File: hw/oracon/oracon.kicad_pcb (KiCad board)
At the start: 2 copper layers, 100 x 134.6 mm, 102 parts, among them J1 DE9_Pins_MountingHoles, J2 SIM_Card, J3 USB_A, J4 Conn_02x20_Odd_Even, J5 USB_C_Receptacle_USB2.0_16P, Q1 SS8050, Q2 SS8050, Q3 SS8050, Q5 SS8050, SW1 SW_Push, U1 TP5100, U2 AMS1117-3.3, U3 ESP32-S3-MINI-1U, U4 CH343P, U5 TPS61022, U6 MAX3232, U7 SIM7022

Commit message: Work on PCB, renamed KiCad project
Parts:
- removed J4: Conn_02x20_Odd_Even, Connector_PinHeader_2.54mm:PinHeader_2x20_P2.54mm_Vertical
- J3: footprint Connector_USB:USB_A_Molex_67643_Horizontal -> kolskypavel:HYC214-USBA04-113; moved to B.Cu
- J5, U7: moved to B.Cu
- moved SW1 180.0 mm to (8.00, 103.5)
- moved J2 174.1 mm to (-5.75, 97.2), turned to 90 degrees
- moved D6 169.4 mm to (7.79, 98.8)
- moved D4 127.3 mm to (-33.0, 83.5), turned to 90 degrees
- moved D3 125.9 mm to (-33.0, 75.2), turned to 90 degrees
- moved D2 124.0 mm to (-32.8, 66.5), turned to 90 degrees
- moved U3 116.7 mm to (2.15, 94.0)
- moved R1 115.6 mm to (35.0, 100.2)
- moved R2 115.6 mm to (35.0, 103.7)
- moved R24 115.6 mm to (35.0, 93.9)
- moved R25 115.6 mm to (35.0, 95.4)
- moved D5 112.7 mm to (-33.0, 92.2), turned to 90 degrees
- moved L1 108.5 mm to (23.0, 95.7)
- moved C15 108.5 mm to (20.1, 94.9)
- moved C16 108.5 mm to (22.5, 96.4)
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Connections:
- J1 pad 2: Net-(U6-T1OUT) -> Net-(U6-R1IN)
- J1 pad 3: Net-(U6-R1IN) -> Net-(U6-T1OUT)
- R32 pad 1: unconnected-(R32-Pad1) -> Net-(J4-In)
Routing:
- net Net-(U6-T1OUT): track 11.4 -> 5.82 mm
- net Net-(U6-R1IN): track 5.82 -> 11.4 mm
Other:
- board size 100 x 134.6 mm -> 97.8 x 134.6 mm

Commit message: PCB layout - init
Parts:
- removed J1: DE9_Pins_MountingHoles, Connector_Dsub:DSUB-9_Pins_Horizontal_P2.77x2.84mm_EdgePinOffset4.94mm_Housed_MountingHolesOffset4.94mm
- added GND: Serial_GND, TestPoint:TestPoint_Pad_D1.5mm, F.Cu at (30.8, 82.8)
- added J4: Conn_Coaxial, kolskypavel:IPEX-SMD_4P-L1.8-W1.7-LS2.0, F.Cu at (-19.8, 64.2)
- added RX: Serial_RX, TestPoint:TestPoint_Pad_D1.5mm, F.Cu at (30.8, 90.0)
- added TX: Serial_TX, TestPoint:TestPoint_Pad_D1.5mm, F.Cu at (30.8, 86.5)
- C10, C11, C12, C13, C14, C18, C19, C20, C21, C22, C8, C9, R10, R11, R7: moved to B.Cu
- C3, C32, C33, C35, C4, C7, L2, R12, R13, R14, R24, R25, R3, U2, U5: moved to F.Cu
- SIM RST: renamed from SW1
- moved C24 184.9 mm to (-21.5, 92.8), turned to 180 degrees
- moved C25 184.2 mm to (-21.5, 93.8)
- moved C26 183.5 mm to (-21.5, 94.8), turned to 180 degrees
- moved C23 178.5 mm to (-18.2, 97.0), turned to -90 degrees
- moved C31 168.3 mm to (4.33, 98.5), turned to 180 degrees
- moved Q3 168.0 mm to (12.7, 97.0), turned to 180 degrees
- moved Q5 166.7 mm to (8.19, 97.3), turned to 180 degrees
- moved R29 162.3 mm to (-18.2, 93.8)
- moved R30 161.6 mm to (-18.2, 94.8)
- moved R28 156.6 mm to (-18.2, 92.8)
- moved R33 152.1 mm to (3.81, 96.5), turned to -90 degrees
- moved C27 150.6 mm to (-13.5, 66.2), turned to -90 degrees
- moved R34 149.8 mm to (4.81, 96.5), turned to 90 degrees
- moved R27 149.1 mm to (11.2, 100.5), turned to -90 degrees
- moved C28 146.3 mm to (-10.0, 66.2), turned to -90 degrees
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- renumbered D4 to BAT, D5 to CHG, D6 to NET, D3 to SIG, J2 to SIM, D2 to STAT
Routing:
- net +3.3V: track 97.9 -> 0.00 mm, vias 5 -> 0
- net CHG_STAT: track 77.5 -> 0.00 mm, vias 4 -> 0
- net STBY_STAT: track 76.7 -> 0.00 mm, vias 2 -> 0
- net PC_RX: track 66.9 -> 0.00 mm, vias 3 -> 0
- net PC_TX: track 66.2 -> 0.00 mm, vias 1 -> 0
- net RST: track 64.5 -> 0.00 mm, vias 5 -> 0
- net +5V: track 62.7 -> 0.00 mm, vias 3 -> 0
- net GPIO0: track 54.8 -> 0.00 mm, vias 3 -> 0
- net USB_SI_P: track 54.5 -> 0.00 mm
- net USB_SI_N: track 54.2 -> 0.00 mm
- net VBUS: track 38.7 -> 0.00 mm, vias 7 -> 0
- net ADC_BATT: track 35.7 -> 0.00 mm, vias 1 -> 0
- net (no net): track 34.0 -> 0.00 mm
- net +BATT: track 21.6 -> 0.00 mm
- net VCC: track 21.2 -> 0.00 mm, vias 7 -> 0
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- removed copper zone on B.Cu, net +5V
- removed copper zone on B.Cu, net +BATT
- removed copper zone on B.Cu, net GND
- removed copper zone on F.Cu, net GND
- removed copper zone on B.Cu, net Net-(D1-K)
- removed copper zone on B.Cu, net Net-(U1-VS)
- removed copper zone on B.Cu, net Net-(U5-SW)
- removed copper zone on B.Cu, net VBUS
- removed copper zone on F.Cu, net VBUS
- removed copper zone on B.Cu, net VCC
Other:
- board size 97.8 x 134.6 mm -> 81 x 56 mm
- board text added: "@kolskypavel/Oracon v0.2"
- board text removed: "@kolskypavel/Oracon v0.1"

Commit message: PCB work, back to basics  :D
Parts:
- C19, C20, C21, C22, U7: moved to F.Cu
- C3, C32, C33, C34, C35, C4, C7, L2, R13, R14, R3, U2, U5: moved to B.Cu
- J5: footprint Connector_USB:USB_C_Receptacle_GCT_USB4105-xx-A_16P_TopMnt_Horizontal -> kolskypavel:HOAUC HYCW412-USBC16-065B; moved to F.Cu
- SW1: renamed from SIM RST
- moved C7 83.0 mm to (94.5, 119.5), turned to 0 degrees
- moved C3 80.0 mm to (92.8, 110.0), turned to 180 degrees
- moved R3 79.2 mm to (92.2, 106.5)
- moved C4 75.1 mm to (89.8, 106.0), turned to 180 degrees
- moved U2 73.2 mm to (60.6, 117.5), turned to 0 degrees
- moved C33 67.2 mm to (56.1, 123.0)
- moved C32 66.0 mm to (55.2, 126.0), turned to 180 degrees
- moved C11 64.8 mm to (54.2, 119.5)
- moved U5 64.0 mm to (53.5, 123.0), turned to 180 degrees
- moved C10 62.8 mm to (52.5, 120.0)
- moved L2 61.4 mm to (51.1, 117.5), turned to 0 degrees
- moved R13 61.3 mm to (51.0, 127.3), turned to 180 degrees
- moved C35 60.7 mm to (50.5, 122.7)
- moved R14 59.2 mm to (49.0, 127.3), turned to 180 degrees
- moved C9 57.3 mm to (46.8, 115.7)
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- renumbered STAT to D2, SIG to D3, BAT to D4, CHG to D5, NET to D6, SIM to J2, TX to TP5, RX to TP6, GND to TP7
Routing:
- net Net-(D3-RK): track 0.00 -> 9.11 mm
- net Net-(U6-R1IN): track 0.00 -> 7.08 mm
- net Net-(D3-GK): track 0.00 -> 6.20 mm
- net Net-(D4-BK): track 0.00 -> 5.95 mm
- net Net-(D4-RK): track 0.00 -> 5.70 mm
- net Net-(U6-T1OUT): track 0.00 -> 5.52 mm
- net Net-(D2-RK): track 0.00 -> 5.40 mm
- net Net-(D5-RK): track 0.00 -> 4.69 mm
- net Net-(D3-BK): track 0.00 -> 3.70 mm
- net Net-(D4-GK): track 0.00 -> 3.45 mm
- net Net-(D2-GK): track 0.00 -> 2.81 mm
- net Net-(D2-BK): track 0.00 -> 2.81 mm
- net Net-(D5-BK): track 0.00 -> 2.60 mm
- net Net-(U6-C2+): track 0.00 -> 2.15 mm
- net Net-(U6-VS-): track 0.00 -> 2.12 mm
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
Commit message: Further PCB work
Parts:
- C12, C13, C14, C18, R7: moved to F.Cu
- C31, Q3, Q5, R12, R26, R27, R33, R34: moved to B.Cu
- moved C7 60.3 mm to (37.7, 99.4)
- moved U2 57.7 mm to (11.2, 87.7), turned to 180 degrees
- moved C3 57.5 mm to (36.8, 96.8), turned to 0 degrees
- moved R3 56.2 mm to (37.3, 94.7), turned to 180 degrees
- moved C4 56.1 mm to (35.2, 92.8)
- moved C32 54.0 mm to (9.85, 96.5), turned to -90 degrees
- moved C34 53.5 mm to (7.80, 96.5), turned to -90 degrees
- moved SW1 52.6 mm to (26.5, 54.8), turned to 0 degrees
- moved TP1 51.9 mm to (41.5, 99.8), turned to 180 degrees
- moved C33 51.6 mm to (11.8, 96.5), turned to -90 degrees
- moved U1 51.5 mm to (33.8, 100.5)
- moved C5 51.5 mm to (32.2, 95.5)
- moved L1 51.5 mm to (27.2, 97.7)
- moved C2 51.5 mm to (31.8, 104.5)
- moved C6 51.4 mm to (34.0, 95.1)
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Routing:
- net LED2_G: track 0.00 -> 46.5 mm, vias 0 -> 1
- net LED2_R: track 0.00 -> 40.5 mm, vias 0 -> 1
- net LED1_G: track 0.00 -> 32.8 mm, vias 0 -> 1
- net NB_RST: track 0.00 -> 32.4 mm, vias 0 -> 1
- net LED1_B: track 1.54 -> 33.8 mm
- net LED1_R: track 0.00 -> 31.9 mm, vias 0 -> 1
- net LED2_B: track 0.00 -> 31.8 mm, vias 0 -> 1
- net VCC: track 0.00 -> 29.8 mm
- net STBY_STAT: track 0.00 -> 26.1 mm, vias 0 -> 1
- net CHG_STAT: track 0.00 -> 23.7 mm, vias 0 -> 1
- net NETLIGHT: track 0.00 -> 23.1 mm, vias 0 -> 1
- net VBUS: track 0.00 -> 21.9 mm, vias 0 -> 1
- net +BATT: track 0.00 -> 18.7 mm
- net +3.3V: track 2.01 -> 14.0 mm
- net RF_ANT: track 0.00 -> 6.52 mm
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- added copper zone on B.Cu, net +5V
- added copper zone on B.Cu, net GND
- added copper zone on B.Cu, net Net-(D1-K)
- added copper zone on B.Cu, net Net-(U5-FB)
- added copper zone on B.Cu, net Net-(U5-SW)
- added copper zone on B.Cu, net VCC

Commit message: Further PCB work - almost ready
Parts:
- R1, R2: moved to F.Cu
- moved U4 16.9 mm to (25.2, 84.3)
- moved Q1 16.8 mm to (30.1, 88.4), turned to 0 degrees
- moved C17 16.5 mm to (22.4, 83.6)
- moved C15 16.5 mm to (26.9, 79.6), turned to 180 degrees
- moved Q2 15.3 mm to (23.6, 88.4)
- moved C16 14.1 mm to (26.9, 81.2)
- moved R9 12.9 mm to (26.6, 88.6)
- moved C24 11.8 mm to (4.92, 81.6)
- moved R8 10.8 mm to (26.6, 87.5), turned to 0 degrees
- moved C14 10.5 mm to (9.75, 79.8), turned to 90 degrees
- moved C12 10.4 mm to (13.3, 79.9), turned to 90 degrees
- moved C13 10.4 mm to (15.3, 80.6), turned to 90 degrees
- moved R7 10.3 mm to (11.5, 80.6), turned to 90 degrees
- moved R28 9.38 mm to (3.85, 81.6)
- moved C25 8.51 mm to (1.73, 81.5), turned to -90 degrees
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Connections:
- U3 pad 16: RS232_TX -> unconnected-(U3-IO12-Pad16)
- U3 pad 17: RS232_RX -> unconnected-(U3-IO13-Pad17)
- U3 pad 23: USB_SI_N -> unconnected-(U3-IO19-Pad23)
- U3 pad 24: USB_SI_P -> unconnected-(U3-IO20-Pad24)
- U3 pad 26: unconnected-(U3-IO26-Pad26) -> CHG_STAT
- U3 pad 27: unconnected-(U3-IO47-Pad27) -> STBY_STAT
- U3 pad 28: STBY_STAT -> LED3_R
- U3 pad 29: CHG_STAT -> LED3_G
- U3 pad 30: unconnected-(U3-IO48-Pad30) -> LED3_B
- U3 pad 33: LED2_G -> LED2_R
- U3 pad 34: LED2_R -> LED2_G
- U3 pad 36: LED1_G -> LED1_R
- U3 pad 37: LED1_R -> LED1_G
- U3 pad 5: unconnected-(U3-IO1-Pad5) -> RS232_TX
- U3 pad 6: LED3_B -> RS232_RX
- U3 pad 7: LED3_G -> USB_SI_N
- U3 pad 8: LED3_R -> USB_SI_P
- U7 pad 15: unconnected-(U7-SIM_DATA-Pad15) -> SIM_DATA
- U7 pad 16: unconnected-(U7-SIM_CLK-Pad16) -> SIM_CLK
- U7 pad 17: unconnected-(U7-SIM_RST-Pad17) -> SIM_RST
- U7 pad 18: unconnected-(U7-SIM_VDD-Pad18) -> SIM_VDD
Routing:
- net NBIOT_RX: track 0.00 -> 59.5 mm, vias 0 -> 1
- net NBIOT_TX: track 0.00 -> 56.8 mm, vias 0 -> 1
- net CHG_STAT: track 23.7 -> 70.7 mm, vias 1 -> 3
- net +5V: track 0.00 -> 47.0 mm
- net STBY_STAT: track 26.1 -> 72.6 mm, vias 1 -> 3
- net USB_SI_N: track 0.00 -> 43.3 mm, vias 0 -> 2
- net USB_SI_P: track 0.00 -> 43.2 mm, vias 0 -> 2
- net SIM_VDD: track 0.00 -> 42.4 mm, vias 0 -> 2
- net PC_TX: track 0.00 -> 38.7 mm, vias 0 -> 3
- net PC_RX: track 0.00 -> 38.1 mm, vias 0 -> 3
- net RS232_RX: track 0.00 -> 36.8 mm, vias 0 -> 1
- net RS232_TX: track 0.00 -> 34.8 mm, vias 0 -> 1
- net VBUS: track 21.9 -> 53.3 mm
- net RST: track 0.00 -> 30.9 mm, vias 0 -> 2
- net SIM_RST: track 0.00 -> 26.8 mm, vias 0 -> 2
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
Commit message: PCB work, paths and zones
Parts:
- moved C20 0.78 mm to (26.0, 64.6)
- moved TP7 0.77 mm to (28.5, 65.2)
- moved TP5 0.76 mm to (28.5, 69.0)
- moved TP6 0.63 mm to (28.4, 72.5)
- moved C9 0.43 mm to (17.3, 89.6)
- moved H3 0.21 mm to (-20.3, 101.8)
- moved R6 0.20 mm to (38.2, 102.2)
- moved H1 0.16 mm to (-20.0, 57.4)
- moved H4 0.10 mm to (41.4, 104.5)
- moved H2 0.09 mm to (41.4, 55.0)
- turned C13 to -90 degrees
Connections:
- C36 pad 1: VBAT -> +3.3V
- C37 pad 1: VBAT -> +3.3V
- U7 pad 1: unconnected-(U7-UART1_TXD-Pad1) -> NBIOT_RX
- U7 pad 2: unconnected-(U7-UART1_RXD-Pad2) -> NBIOT_TX
- U7 pad 22: NBIOT_RX -> unconnected-(U7-UART0_TXD-Pad22)
- U7 pad 23: NBIOT_TX -> unconnected-(U7-UART0_RXD-Pad23)
- U7 pad 34: VBAT -> +3.3V
- U7 pad 35: VBAT -> +3.3V
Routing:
- net +3.3V: track 23.9 -> 175.9 mm, vias 0 -> 8
- net VBUS: track 53.3 -> 157.2 mm, vias 1 -> 3
- net RST: track 30.9 -> 57.3 mm, vias 2 -> 4
- net VCC: track 6.62 -> 30.5 mm
- net NBIOT_RX: track 59.5 -> 43.0 mm
- net NBIOT_TX: track 56.8 -> 42.3 mm
- net VBAT: track 8.17 -> 0.00 mm
- net Net-(U1-VS): track 9.38 -> 14.0 mm
- net +5V: track 47.0 -> 51.0 mm
- net PC_TX: track 38.7 -> 40.0 mm
- net PC_RX: track 38.1 -> 38.9 mm
- net Net-(U6-T1OUT): track 5.52 -> 6.26 mm
- net (no net): track 0.65 -> 0.00 mm
- net RF_ANT: track 6.52 -> 5.87 mm
- net DTR: track 3.29 -> 2.67 mm
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- added copper zone on F.Cu, net GND

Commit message: Some PCB restruct
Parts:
- C12, C13: moved to B.Cu
- moved C13 11.3 mm to (5.98, 87.1), turned to 90 degrees
- moved C12 9.83 mm to (8.76, 88.6), turned to -90 degrees
- moved C10 3.56 mm to (22.9, 86.9), turned to 0 degrees
- moved R6 3.08 mm to (37.1, 105.1)
- moved C8 2.77 mm to (22.2, 89.6)
- moved C9 2.77 mm to (20.1, 89.8)
- moved U2 2.77 mm to (14.7, 87.7)
- moved C11 2.52 mm to (19.8, 85.1)
- moved H1 2.49 mm to (-22.3, 58.5)
- moved H3 2.20 mm to (-22.2, 100.7)
- moved C3 1.22 mm to (36.8, 95.6)
- moved H2 0.81 mm to (41.3, 55.8)
- moved R10 0.81 mm to (1.67, 101.2)
- moved R11 0.81 mm to (0.69, 101.2)
- moved C16 0.81 mm to (27.7, 81.5)
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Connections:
- J2 pad CD: (no net) -> unconnected-(J2-PadCD)
- J2 pad SH: (no net) -> GND
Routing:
- net VCC: track 30.5 -> 42.6 mm
- net +5V: track 51.0 -> 62.2 mm
- net +3.3V: track 175.9 -> 166.6 mm, vias 8 -> 10
- net GND: track 0.00 -> 4.25 mm, vias 0 -> 5
- net NTC: track 3.94 -> 6.94 mm
- net USB_PC_P: track 18.4 -> 21.0 mm
- net USB_SI_P: track 43.2 -> 41.1 mm
- net LED3_B: track 26.0 -> 27.9 mm
- net LED3_R: track 28.0 -> 29.9 mm
- net LED3_G: track 27.0 -> 28.9 mm
- net VBUS: track 157.2 -> 159.0 mm
- net USB_SI_N: track 43.0 -> 41.2 mm
- net USB_PC_N: track 21.8 -> 20.3 mm
- net RST: track 57.3 -> 58.7 mm
- net RS232_RX: track 36.8 -> 35.7 mm
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
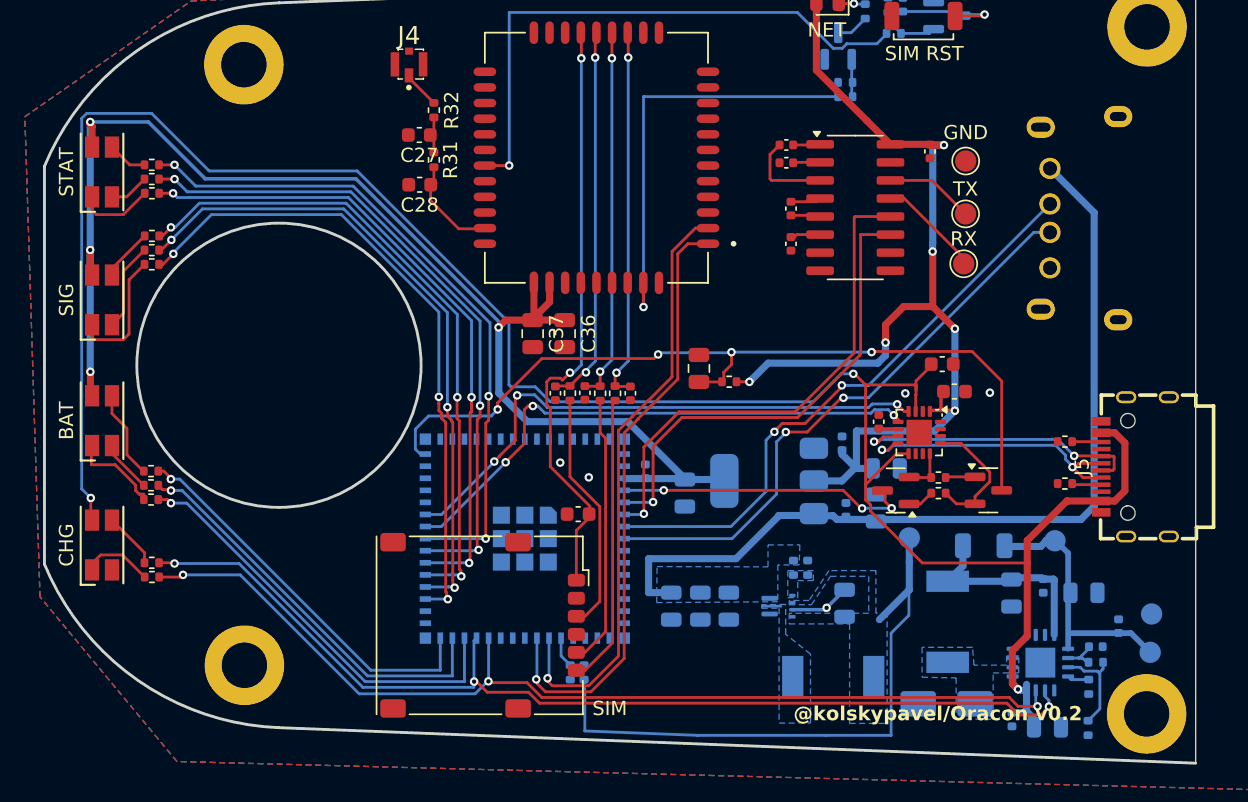
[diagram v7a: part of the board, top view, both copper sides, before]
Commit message: Rerouted some ESP pins
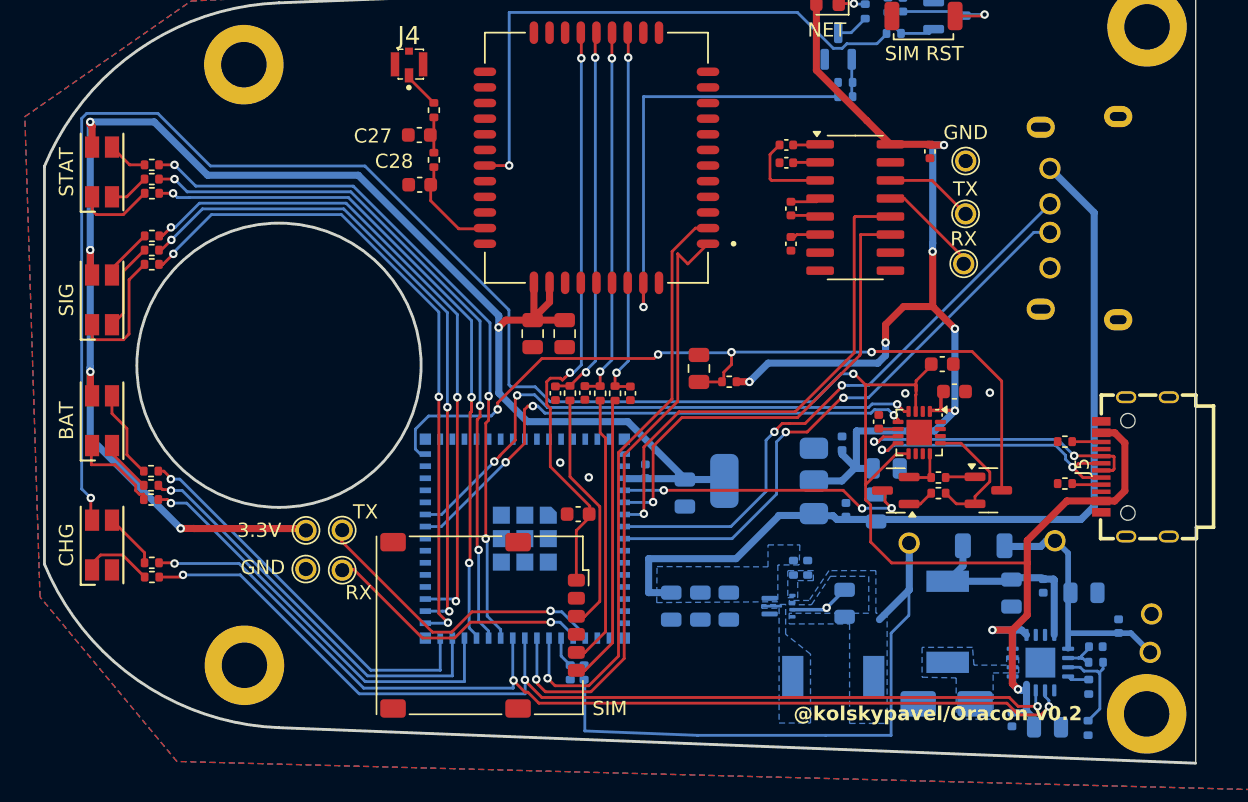
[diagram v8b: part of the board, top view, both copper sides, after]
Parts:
- added H5: SI_TX, TestPoint:TestPoint_Pad_D1.5mm, F.Cu at (-15.3, 91.2)
- added H6: SI_RX, TestPoint:TestPoint_Pad_D1.5mm, F.Cu at (-15.3, 94.0)
- added H7: SI_GND, TestPoint:TestPoint_Pad_D1.5mm, F.Cu at (-17.9, 93.9)
- added H8: SI_3.3V, TestPoint:TestPoint_Pad_D1.5mm, F.Cu at (-17.9, 91.2)
- moved TP4 0.36 mm to (24.5, 92.1)
- turned R14 to 90 degrees
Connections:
- U3 pad 18: unconnected-(U3-IO14-Pad18) -> SI_TX
- U3 pad 19: unconnected-(U3-IO15-Pad19) -> SI_RX
- U3 pad 23: unconnected-(U3-IO19-Pad23) -> CHG_STAT
- U3 pad 24: unconnected-(U3-IO20-Pad24) -> STBY_STAT
- U3 pad 25: unconnected-(U3-IO21-Pad25) -> LED1_B
- U3 pad 26: CHG_STAT -> LED1_G
- U3 pad 27: STBY_STAT -> LED1_R
- U3 pad 31: unconnected-(U3-IO35-Pad31) -> LED2_R
- U3 pad 32: unconnected-(U3-IO36-Pad32) -> LED2_G
- U3 pad 33: LED2_R -> LED2_B
- U3 pad 34: LED2_G -> unconnected-(U3-IO38-Pad34)
- U3 pad 35: LED2_B -> unconnected-(U3-IO39-Pad35)
- U3 pad 36: LED1_R -> unconnected-(U3-IO40-Pad36)
- U3 pad 37: LED1_G -> unconnected-(U3-IO41-Pad37)
- U3 pad 38: LED1_B -> unconnected-(U3-IO42-Pad38)
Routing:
- net +3.3V: track 166.6 -> 189.3 mm, vias 10 -> 11
- net SI_TX: track 0.00 -> 22.0 mm, vias 0 -> 1
- net SI_RX: track 0.00 -> 19.3 mm, vias 0 -> 1
- net VBUS: track 159.0 -> 166.1 mm, vias 3 -> 4
- net LED1_B: track 47.5 -> 50.6 mm
- net LED1_G: track 46.7 -> 49.7 mm
- net LED1_R: track 46.8 -> 49.3 mm
- net LED2_R: track 46.1 -> 47.8 mm
- net LED2_B: track 46.3 -> 47.6 mm
- net LED2_G: track 46.0 -> 47.1 mm
- net NBIOT_RX: track 43.0 -> 43.6 mm
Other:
- board text added: "3.3V"
- board text added: "GND"
- board text added: "RX"
- board text added: "TX"
